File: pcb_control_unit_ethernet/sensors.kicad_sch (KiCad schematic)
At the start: 17 parts, among them J23 Weight, Q4 BC807, U9 HX711

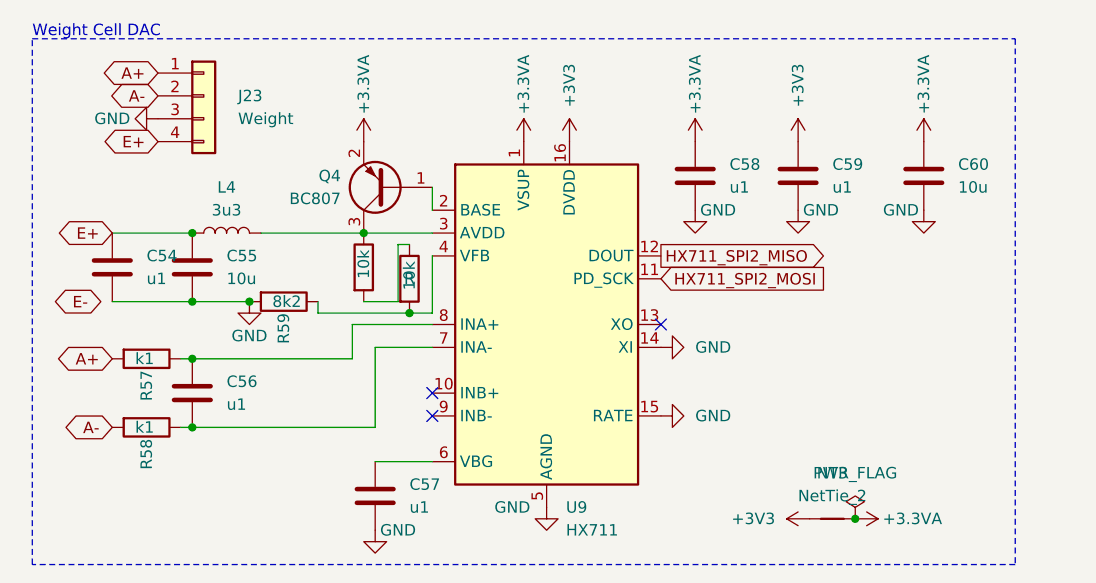
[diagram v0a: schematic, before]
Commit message: First time zero errors, but bad layout
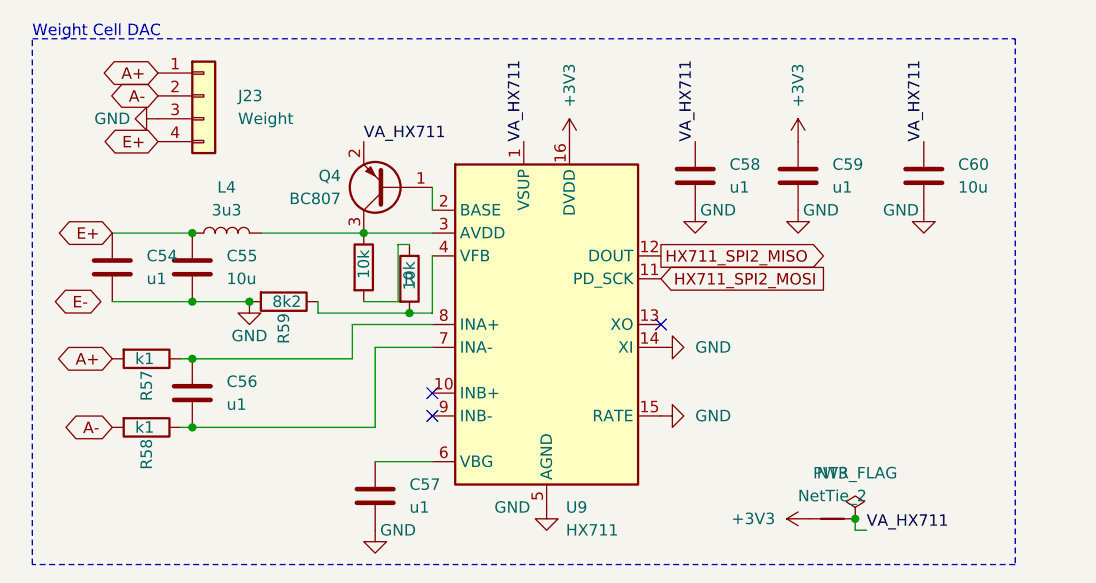
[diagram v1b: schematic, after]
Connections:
- net +3.3VA renamed VA_HX711

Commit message: EtherCAT + HX711
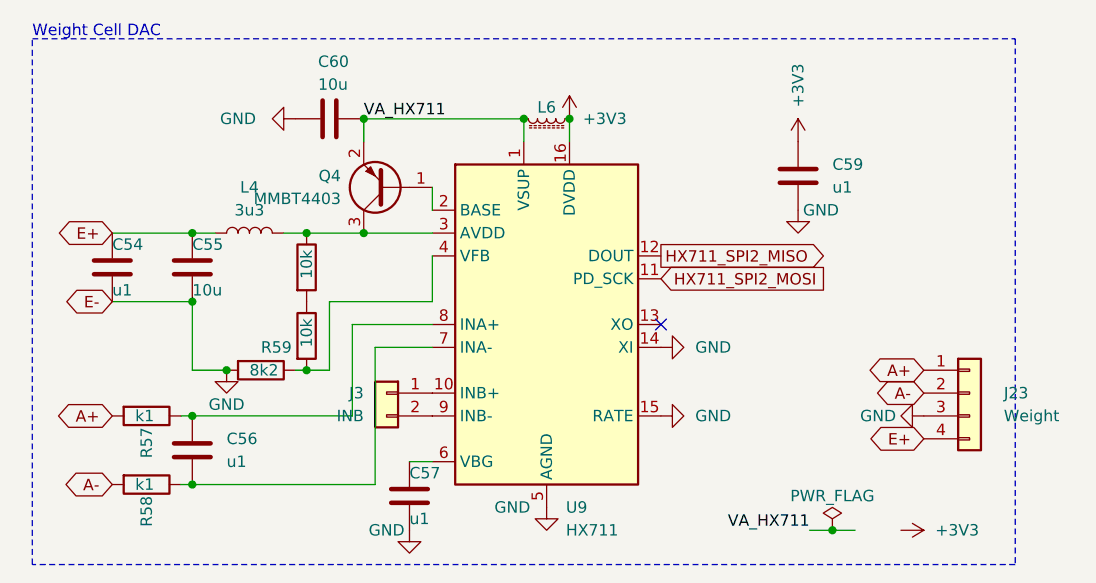
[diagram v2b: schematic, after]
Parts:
- removed C58: u1, Capacitor_SMD:C_0402_1005Metric, symbol Device:C
- removed NT3: NetTie_2, NetTie:NetTie-2_SMD_Pad0.5mm, symbol Device:NetTie_2
- added J3: INB, Connector_JST:JST_XH_B2B-XH-A_1x02_P2.50mm_Vertical, symbol Connector_Generic:Conn_01x02
- added L6: 600R@100M, Inductor_SMD:L_0603_1608Metric, symbol Device:L_Ferrite_Small
- Q4: value BC807 -> MMBT4403
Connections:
- net +3V3: now also L6.1
- net VA_HX711: now also L6.2
- net at U9.10 (INB+): now also J3.1 (Pin_1)
- net at U9.9 (INB-): now also J3.2 (Pin_2)
- no-connect marks 3 -> 1
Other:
- moved on the sheet: C56, C57, C60, J23, L4, R57, R58, R59

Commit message: WIP
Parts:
- R59: value 8k2 -> 10k
- R60: value 10k -> 4k7
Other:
- note added: "Recalculate voltage divisor -->target voltage 3V"
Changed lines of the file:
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@@
+		)
+	)
+	(text "Recalculate voltage divisor -->target voltage 3V"
+		(exclude_from_sim no)
+		(at 43.18 44.45 0)
+		(effects
+			(font
+				(size 1.27 1.27)
+			)
 		)
 	)
@@
 			)
 		)
-		(property "Value" "8k2"
+		(property "Value" "10k"
 			(at 39.37 53.34 90)
 			(effects
@@
 			)
 		)
-		(property "Value" "10k"
+		(property "Value" "4k7"
 			(at 45.72 43.18 90)
 			(effects
